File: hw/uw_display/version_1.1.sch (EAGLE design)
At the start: 99 parts, among them J2 SWD, J4 USB, J5 UART, U1 LPC1785, U2 MCP2551, U3 AS4C4M16SA, U4 W25Q32FV, U5 MIC5247-1.8YM5, U6 TVP5150AM1, U7 TVP5150AM1, X1 20MHz, X2 34.768kHz, X3 14.31MHz, X4 14.31 MHz, Y1 BUZZER

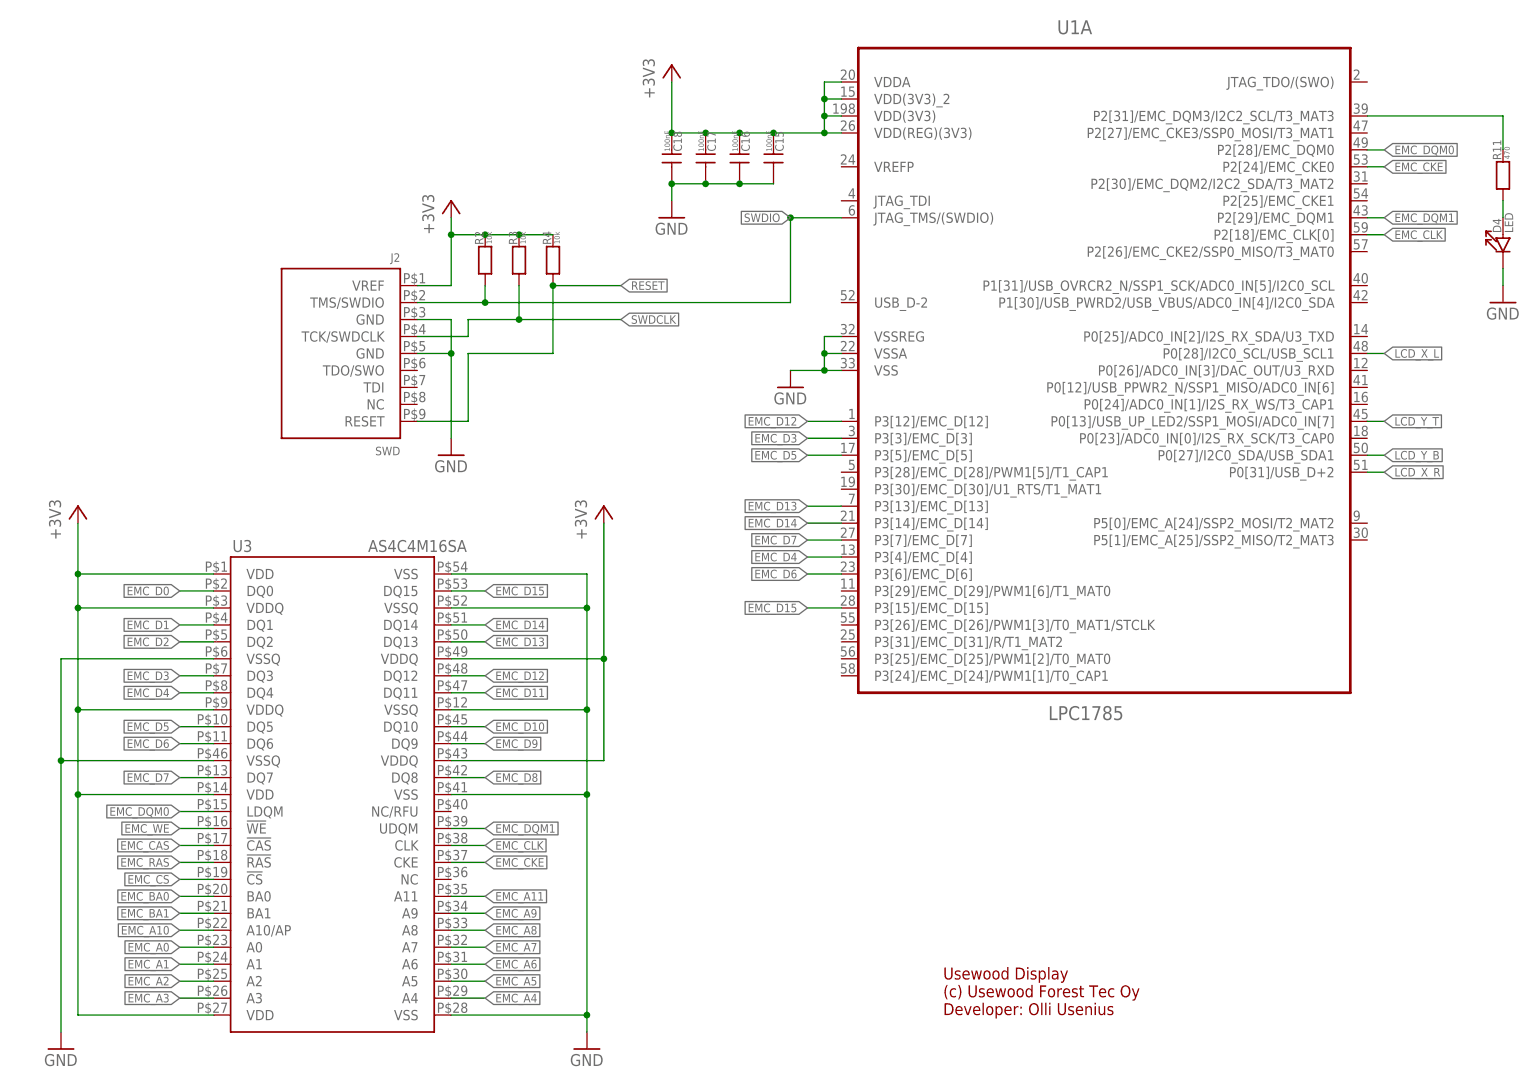
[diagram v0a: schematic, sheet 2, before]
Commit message: Start developing the display SW
   - Testing freertos
   - UART, timers and gpios are working
   - Add uGUI library to ui directory
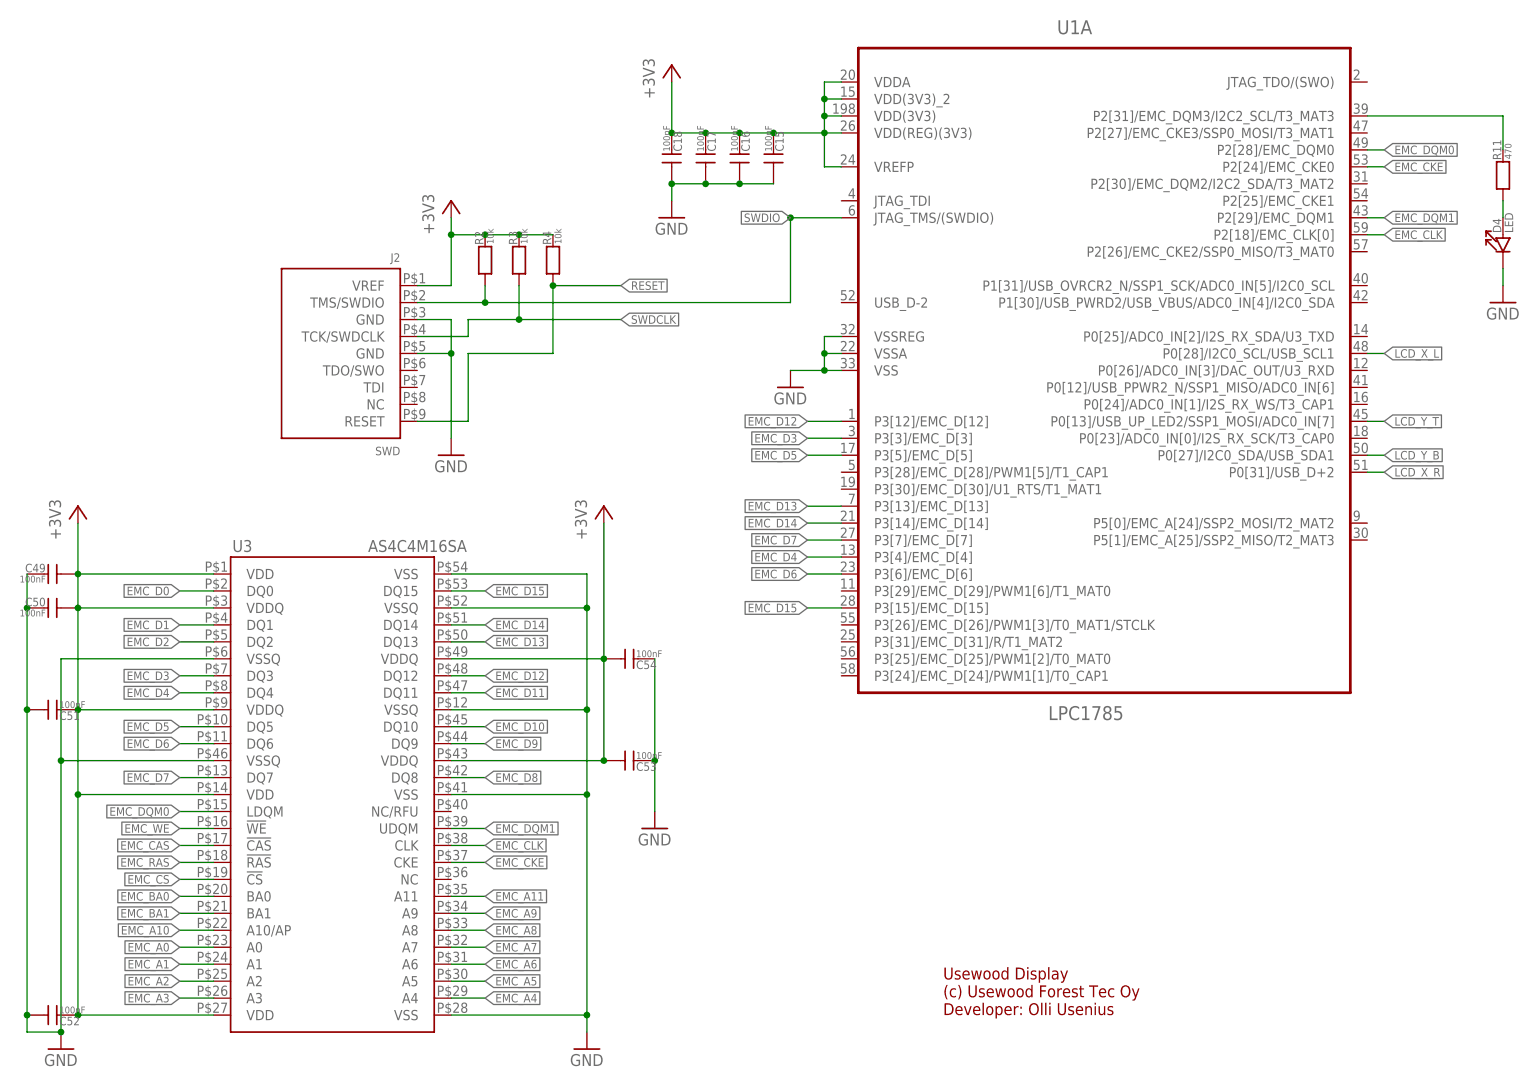
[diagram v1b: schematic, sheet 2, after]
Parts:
- added C49, C50, C51, C52, C53, C54: 100nF, usevolt:CAP_0603
- added R7: 10k, usevolt:RES_0603
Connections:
- new net ISP: R7.P$2, U1C.P2[10]/!EINT0!/NMI
- net +3V3: now also C49.P$1, C50.P$1, C51.P$2, C52.P$2, C53.P$1, C54.P$1, R7.P$1, U1A.VREFP
- net GND: now also C49.P$2, C50.P$2, C51.P$1, C52.P$1, C53.P$2, C54.P$2
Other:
- moved on the sheet: J5
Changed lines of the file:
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@@
 <part name="R6" library="usevolt" deviceset="RES" device="_0603"/>
 <part name="P+15" library="supply1" deviceset="+5V" device=""/>
+<part name="R7" library="usevolt" deviceset="RES" device="_0603" value="10k"/>
+<part name="+3V14" library="supply1" deviceset="+3V3" device=""/>
+<part name="C49" library="usevolt" deviceset="CAP" device="_0603" value="100nF"/>
+<part name="C50" library="usevolt" deviceset="CAP" device="_0603" value="100nF"/>
+<part name="C51" library="usevolt" deviceset="CAP" device="_0603" value="100nF"/>
+<part name="C52" library="usevolt" deviceset="CAP" device="_0603" value="100nF"/>
+<part name="C53" library="usevolt" deviceset="CAP" device="_0603" value="100nF"/>
+<part name="C54" library="usevolt" deviceset="CAP" device="_0603" value="100nF"/>
+<part name="GND31" library="supply1" deviceset="GND" device=""/>
 </parts>
 <sheets>
@@
 <instance part="GND18" gate="1" x="30.48" y="10.16"/>
 <instance part="GND19" gate="1" x="109.22" y="10.16"/>
+<instance part="C49" gate="G$1" x="27.94" y="81.28" rot="R180"/>
+<instance part="C50" gate="G$1" x="27.94" y="76.2" rot="R180"/>
+<instance part="C51" gate="G$1" x="30.48" y="60.96"/>
+<instance part="C52" gate="G$1" x="30.48" y="15.24"/>
+<instance part="C53" gate="G$1" x="116.84" y="53.34"/>
+<instance part="C54" gate="G$1" x="116.84" y="68.58"/>
+<instance part="GND31" gate="1" x="119.38" y="43.18"/>
 </instances>
 <busses>
@@
 <wire x1="30.48" y1="68.58" x2="53.34" y2="68.58" width="0.1524" layer="91"/>
 <junction x="30.48" y="53.34"/>
+<wire x1="30.48" y1="12.7" x2="25.4" y2="12.7" width="0.1524" layer="91"/>
+<junction x="30.48" y="12.7"/>
+<pinref part="C52" gate="G$1" pin="P$1"/>
+<wire x1="25.4" y1="12.7" x2="25.4" y2="15.24" width="0.1524" layer="91"/>
+<pinref part="C51" gate="G$1" pin="P$1"/>
+<wire x1="25.4" y1="15.24" x2="25.4" y2="60.96" width="0.1524" layer="91"/>
+<junction x="25.4" y="15.24"/>
+<pinref part="C50" gate="G$1" pin="P$2"/>
+<wire x1="25.4" y1="60.96" x2="25.4" y2="76.2" width="0.1524" layer="91"/>
+<junction x="25.4" y="60.96"/>
+<pinref part="C49" gate="G$1" pin="P$2"/>
+<wire x1="25.4" y1="76.2" x2="25.4" y2="81.28" width="0.1524" layer="91"/>
+<junction x="25.4" y="76.2"/>
+</segment>
+<segment>
+<pinref part="C54" gate="G$1" pin="P$2"/>
+<pinref part="C53" gate="G$1" pin="P$2"/>
+<wire x1="119.38" y1="68.58" x2="119.38" y2="53.34" width="0.1524" layer="91"/>
+<wire x1="119.38" y1="53.34" x2="119.38" y2="45.72" width="0.1524" layer="91"/>
+<junction x="119.38" y="53.34"/>
+<pinref part="GND31" gate="1" pin="GND"/>
 </segment>
 </net>
@@
 <wire x1="121.92" y1="154.94" x2="121.92" y2="147.32" width="0.1524" layer="91"/>
 <junction x="121.92" y="147.32"/>
+<pinref part="U1" gate="A" pin="VREFP"/>
+<wire x1="147.32" y1="142.24" x2="144.78" y2="142.24" width="0.1524" layer="91"/>
+<wire x1="144.78" y1="142.24" x2="144.78" y2="147.32" width="0.1524" layer="91"/>
 </segment>
 <segment>
@@
 <wire x1="33.02" y1="15.24" x2="53.34" y2="15.24" width="0.1524" layer="91"/>
 <junction x="33.02" y="48.26"/>
+<pinref part="C49" gate="G$1" pin="P$1"/>
+<pinref part="C50" gate="G$1" pin="P$1"/>
+<pinref part="C51" gate="G$1" pin="P$2"/>
+<pinref part="C52" gate="G$1" pin="P$2"/>
+<junction x="33.02" y="15.24"/>
 </segment>
 <segment>
@@
 <wire x1="111.76" y1="53.34" x2="88.9" y2="53.34" width="0.1524" layer="91"/>
 <junction x="111.76" y="68.58"/>
+<pinref part="C53" gate="G$1" pin="P$1"/>
+<junction x="111.76" y="53.34"/>
+<pinref part="C54" gate="G$1" pin="P$1"/>
 </segment>
 </net>
@@
 <instance part="R19" gate="G$1" x="175.26" y="48.26" rot="R90"/>
 <instance part="+3V13" gate="G$1" x="175.26" y="60.96"/>
+<instance part="R7" gate="G$1" x="198.12" y="127" rot="R270"/>
+<instance part="+3V14" gate="G$1" x="198.12" y="134.62"/>
 </instances>
 <busses>
@@
 <wire x1="172.72" y1="55.88" x2="172.72" y2="50.8" width="0.1524" layer="91"/>
 </segment>
+<segment>
+<pinref part="R7" gate="G$1" pin="P$1"/>
+<pinref part="+3V14" gate="G$1" pin="+3V3"/>
+<wire x1="198.12" y1="129.54" x2="198.12" y2="132.08" width="0.1524" layer="91"/>
+</segment>
 </net>
 <net name="GND" class="0">
@@
 </segment>
 </net>
+<net name="ISP" class="0">
+<segment>
+<pinref part="U1" gate="C" pin="P2[10]/!EINT0!/NMI"/>
+<pinref part="R7" gate="G$1" pin="P$2"/>
+<wire x1="198.12" y1="121.92" x2="165.1" y2="121.92" width="0.1524" layer="91"/>
+<label x="190.5" y="121.92" size="1.27" layer="95"/>
+</segment>
+</net>

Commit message: Display runs now with uw_bootloader
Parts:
- U4: device usevolt:WINDBOND_W25Q32FV_SOIC8 -> usevolt:WINDBOND_W25Q32FV_SOIC8_W
- U5: device usevolt:MICREL_MIC5247-1.8YM5_SOT23-5 -> usevolt:REG_MICREL_MIC5247-1.8YM5_SOT23-5
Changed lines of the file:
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@@
 <part name="U2" library="usevolt" deviceset="MCP2551" device="_SOIC8" value="MCP2551"/>
 <part name="U$2" library="usevolt" deviceset="HEADER12" device="_MX120G" value="MX120G"/>
-<part name="U4" library="usevolt" deviceset="WINDBOND_W25Q32FV" device="_SOIC8" value="W25Q32FV"/>
+<part name="U4" library="usevolt" deviceset="WINDBOND_W25Q32FV" device="_SOIC8_W" value="W25Q32FV"/>
 <part name="+3V10" library="supply1" deviceset="+3V3" device=""/>
 <part name="GND20" library="supply1" deviceset="GND" device=""/>
@@
 <part name="+3V11" library="supply1" deviceset="+3V3" device=""/>
 <part name="FRAME6" library="frames" deviceset="A4L-LOC" device=""/>
-<part name="U5" library="usevolt" deviceset="MICREL_MIC5247-1.8YM5" device="_SOT23-5" value="MIC5247-1.8YM5"/>
+<part name="U5" library="usevolt" deviceset="REG_MICREL_MIC5247-1.8YM5" device="_SOT23-5" value="MIC5247-1.8YM5"/>
 <part name="P+7" library="supply1" deviceset="+5V" device=""/>
 <part name="P+8" library="supply1" deviceset="V+" device=""/>

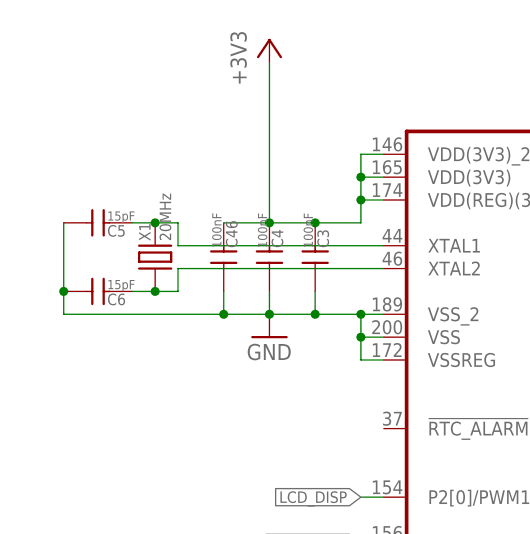
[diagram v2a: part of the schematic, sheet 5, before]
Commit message: Corrected HW connector bolt sizes
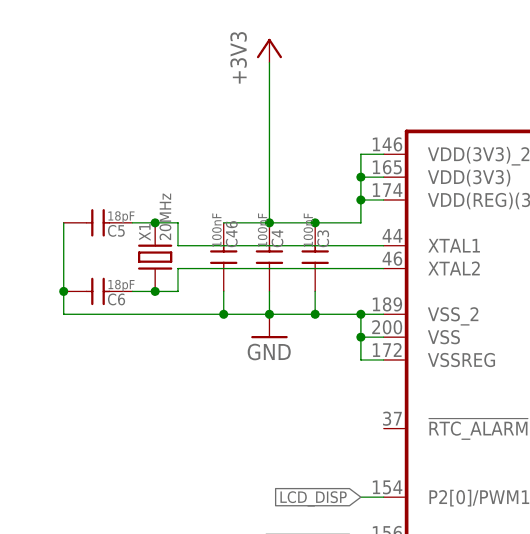
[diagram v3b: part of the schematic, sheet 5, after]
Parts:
- C5, C6: value 15pF -> 18pF
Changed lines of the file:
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@@
 <?xml version="1.0" encoding="utf-8"?>
 <!DOCTYPE eagle SYSTEM "eagle.dtd">
-<eagle version="7.2.0">
+<eagle version="7.6.0">
 <drawing>
 <settings>
@@
 <setting verticaltext="up"/>
 </settings>
-<grid distance="0.1" unitdist="inch" unit="inch" style="lines" multiple="1" display="no" altdistance="0.01" altunitdist="inch" altunit="inch"/>
+<grid distance="0.1" unitdist="inch" unit="mm" style="lines" multiple="1" display="no" altdistance="0.01" altunitdist="inch" altunit="inch"/>
 <layers>
 <layer number="1" name="Top" color="4" fill="1" visible="no" active="no"/>
@@
 <part name="GND4" library="supply1" deviceset="GND" device=""/>
 <part name="X1" library="usevolt" deviceset="XTAL_7A-20.000MAAJ-T" device="" value="20MHz"/>
-<part name="C5" library="usevolt" deviceset="CAP" device="_0603" value="15pF"/>
-<part name="C6" library="usevolt" deviceset="CAP" device="_0603" value="15pF"/>
+<part name="C5" library="usevolt" deviceset="CAP" device="_0603" value="18pF"/>
+<part name="C6" library="usevolt" deviceset="CAP" device="_0603" value="18pF"/>
 <part name="+3V4" library="supply1" deviceset="+3V3" device=""/>
 <part name="GND5" library="supply1" deviceset="GND" device=""/>
